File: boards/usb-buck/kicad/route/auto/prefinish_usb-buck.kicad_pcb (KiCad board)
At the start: 4 copper layers, 50 x 40 mm, 28 parts, among them J1 USB Micro-B receptacle SMD, J2 1x4 2.54mm male THT, SW1 SMD tactile switch, U1 STM32F103C8T6, U2 AP63203QWU-7, U3 USBLC6-2SC6, Y1 8MHz 20pF

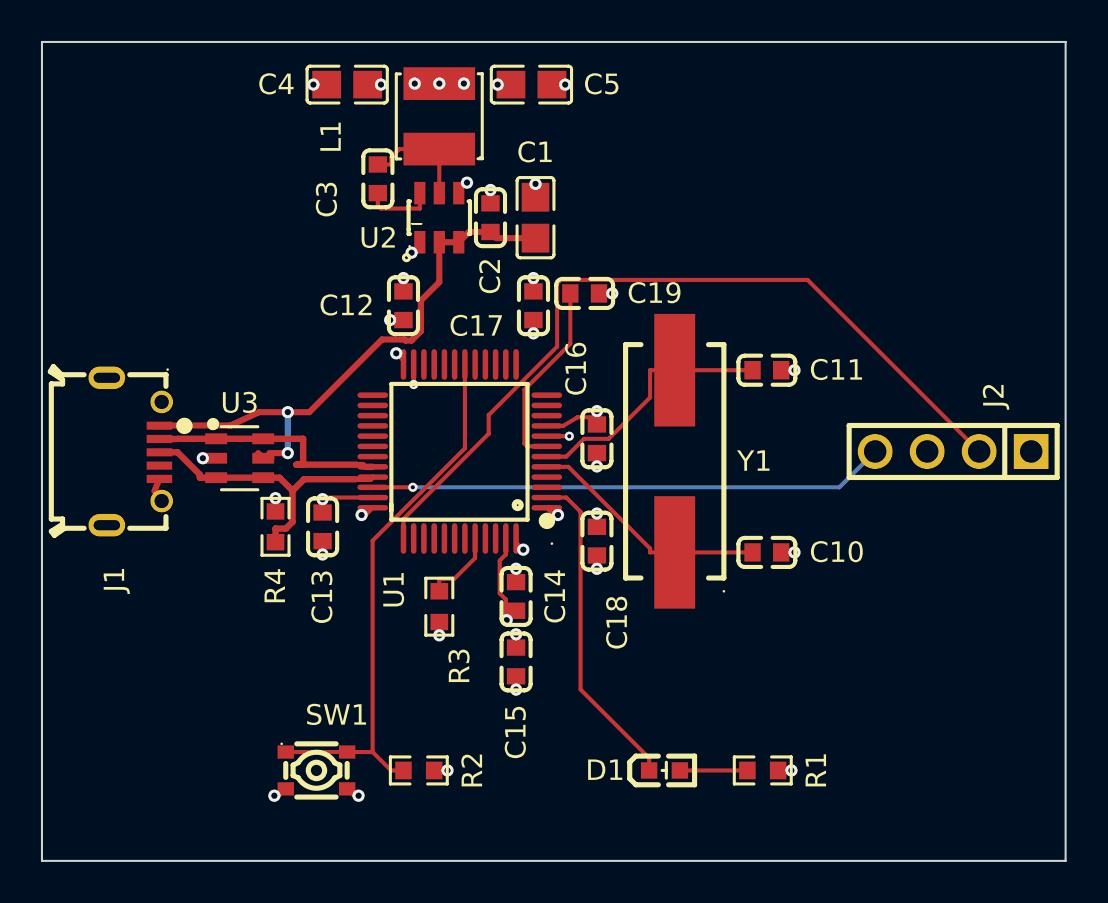
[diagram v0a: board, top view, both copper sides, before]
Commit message: ai-ee usb-buck: drc_routed pass (4L chain; 4 router-found defects fixed in-run)
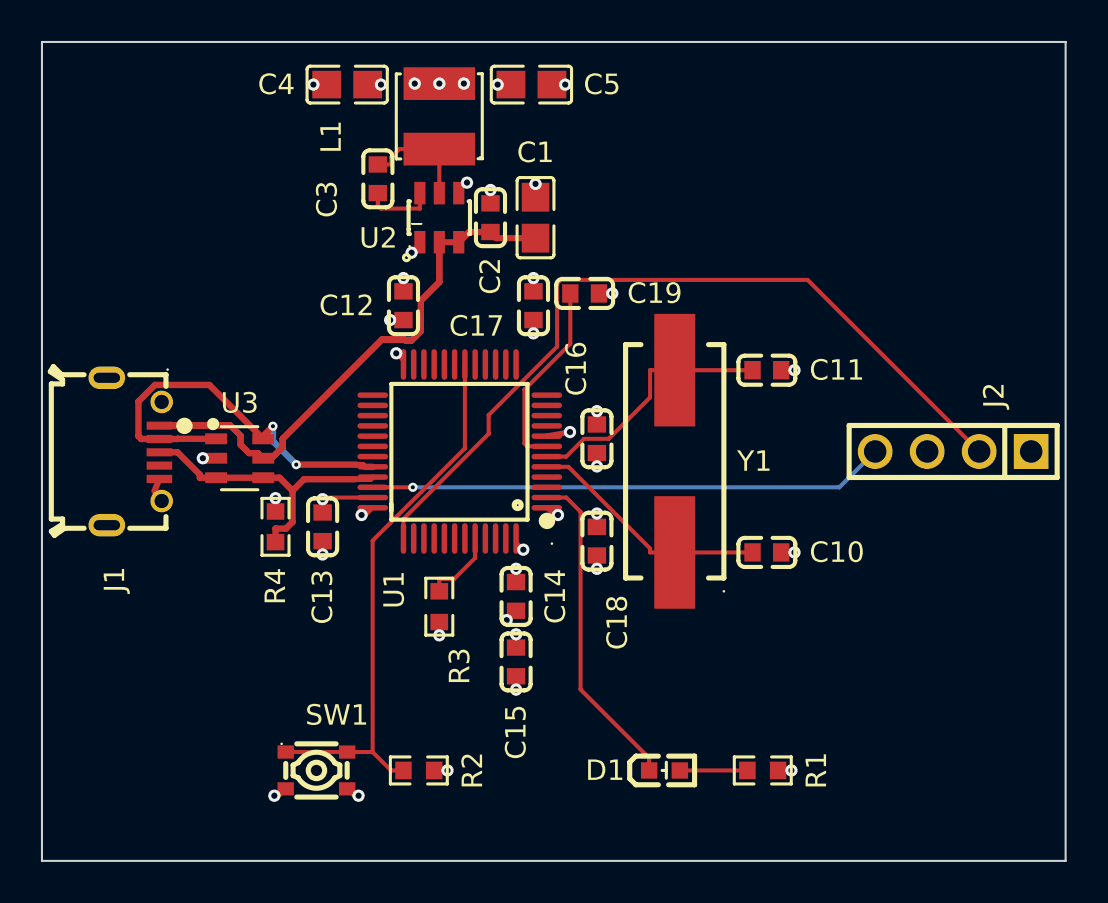
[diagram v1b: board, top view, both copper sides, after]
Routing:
- net VBUS: track 28.0 -> 47.9 mm, vias 2 -> 0
- net GND: track 29.8 -> 15.5 mm, vias 21 -> 20
- net /USB_DM: track 12.4 -> 20.0 mm, vias 0 -> 2
- net +3V3: track 16.8 -> 11.2 mm
